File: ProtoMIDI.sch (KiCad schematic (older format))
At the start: 10 parts, among them J1 DIN-5_180degree, U1 6N137

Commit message: Draft schematic (incomplete).
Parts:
- removed C1, C2, C3: 100n, symbol Device:C
- removed D1: 1N4148, symbol Device:D
- removed FB1, FB2: 1k@100MHz, symbol Device:Ferrite_Bead
- removed J1: DIN-5_180degree, symbol Connector:DIN-5_180degree
- removed R1, R2: 220, symbol Device:R
- removed U1: 6N137, Package_DIP:DIP-8_W7.62mm_SMDSocket_SmallPads, symbol Isolator:6N137
- added C10, C11, C14, C15, C21: 1u, Capacitor_SMD:C_0603_1608Metric, symbol Device:C
- added C12, C13: 27p, Capacitor_SMD:C_0603_1608Metric, symbol Device:C
- added C16, C17, C18, C19, C6, C7, C8: 100n, Capacitor_SMD:C_0603_1608Metric, symbol Device:C
- added C20: 10n, Capacitor_SMD:C_0603_1608Metric, symbol Device:C
- added C4: 1u, symbol Device:C
- added C5, C9: 100n, symbol Device:C
- added J10, J12, J13, J14, J15, J16, J17, J18, J19, J3, J4, J5, J6, J7, J8, J9: AudioJack2_SwitchT, Local:PJ398SM, symbol Connector:AudioJack2_SwitchT
- added J11: Conn_01x09_Male, Connector_PinHeader_2.54mm:PinHeader_1x09_P2.54mm_Vertical, symbol Connector:Conn_01x09_Male
- added J2: Conn_01x04_Male, Connector_PinHeader_2.54mm:PinHeader_1x04_P2.54mm_Vertical, symbol Connector:Conn_01x04_Male
- added R10, R11, R12, R13, R14, R15, R16, R8, R9: 1k, Resistor_SMD:R_0603_1608Metric, symbol Device:R
- added R3: 10k, Resistor_SMD:R_0603_1608Metric, symbol Device:R
- added R4: 470, Resistor_SMD:R_0603_1608Metric, symbol Device:R
- added R5, R6, R7: 4k7, Resistor_SMD:R_0603_1608Metric, symbol Device:R
- added SW1: SW_Push, Button_Switch_THT:SW_PUSH_6mm, symbol Switch:SW_Push
- added SW2: SW_Push, symbol Switch:SW_Push
- added SW3: Rotary_Encoder_Switch, Rotary_Encoder:RotaryEncoder_Alps_EC11E-Switch_Vertical_H20mm, symbol Device:Rotary_Encoder_Switch
- added U03: STM32G071RBTx, LQFP64, symbol STM32G071RBTx:STM32G071RBTx
- added U1: AT25xxx, Package_SO:TSSOP-8_4.4x3mm_P0.65mm, symbol Memory_EEPROM:AT25xxx
- added U4: IPS240x240, Local:IPS240x240, symbol Local:IPS240x240
- added U5: 74AHCT244, Package_SO:TSSOP-20_4.4x6.5mm_P0.65mm, symbol 74xx:74HCT244
- added Y1: 8MHz, Crystal:Crystal_SMD_5032-4Pin_5.0x3.2mm, symbol Device:Crystal_GND24_Small
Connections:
- net labels added: +3.3V, +3.3VA, +5V, CV1, CV2, CV3, CV4, CV5, CV6, CV7, CV8, DAC1_CH1, DAC1_CH2, ENC_CH1, ENC_CH2, ENC_SW, GNDA, LED1, LED2, LED3, LED4, LED5, LED6, LED7, LED8, MEM_CS, MEM_MISO, MEM_MOSI, MEM_SCK, RESET, SPI1_MISO, SPI1_MOSI, SPI1_SCK, SPI2_MISO, SPI2_MOSI, SPI2_SCK, SW1, SW2, SW3, SW4, SW5, SW6, SW7, SW8, SWCLK, SWDIO, TFT+, TFT-, TFT_DC, TFT_RES, TRIG0, TRIG1, TRIG2, TRIG3, TRIG4, TRIG5, TRIG6, TRIG7, TRIG8, USART3_RX, USART3_TX, VREF
- wire segments 32 -> 238
- no-connect marks 0 -> 16
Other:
- note removed: "FIXME: Connect\ncase here!"

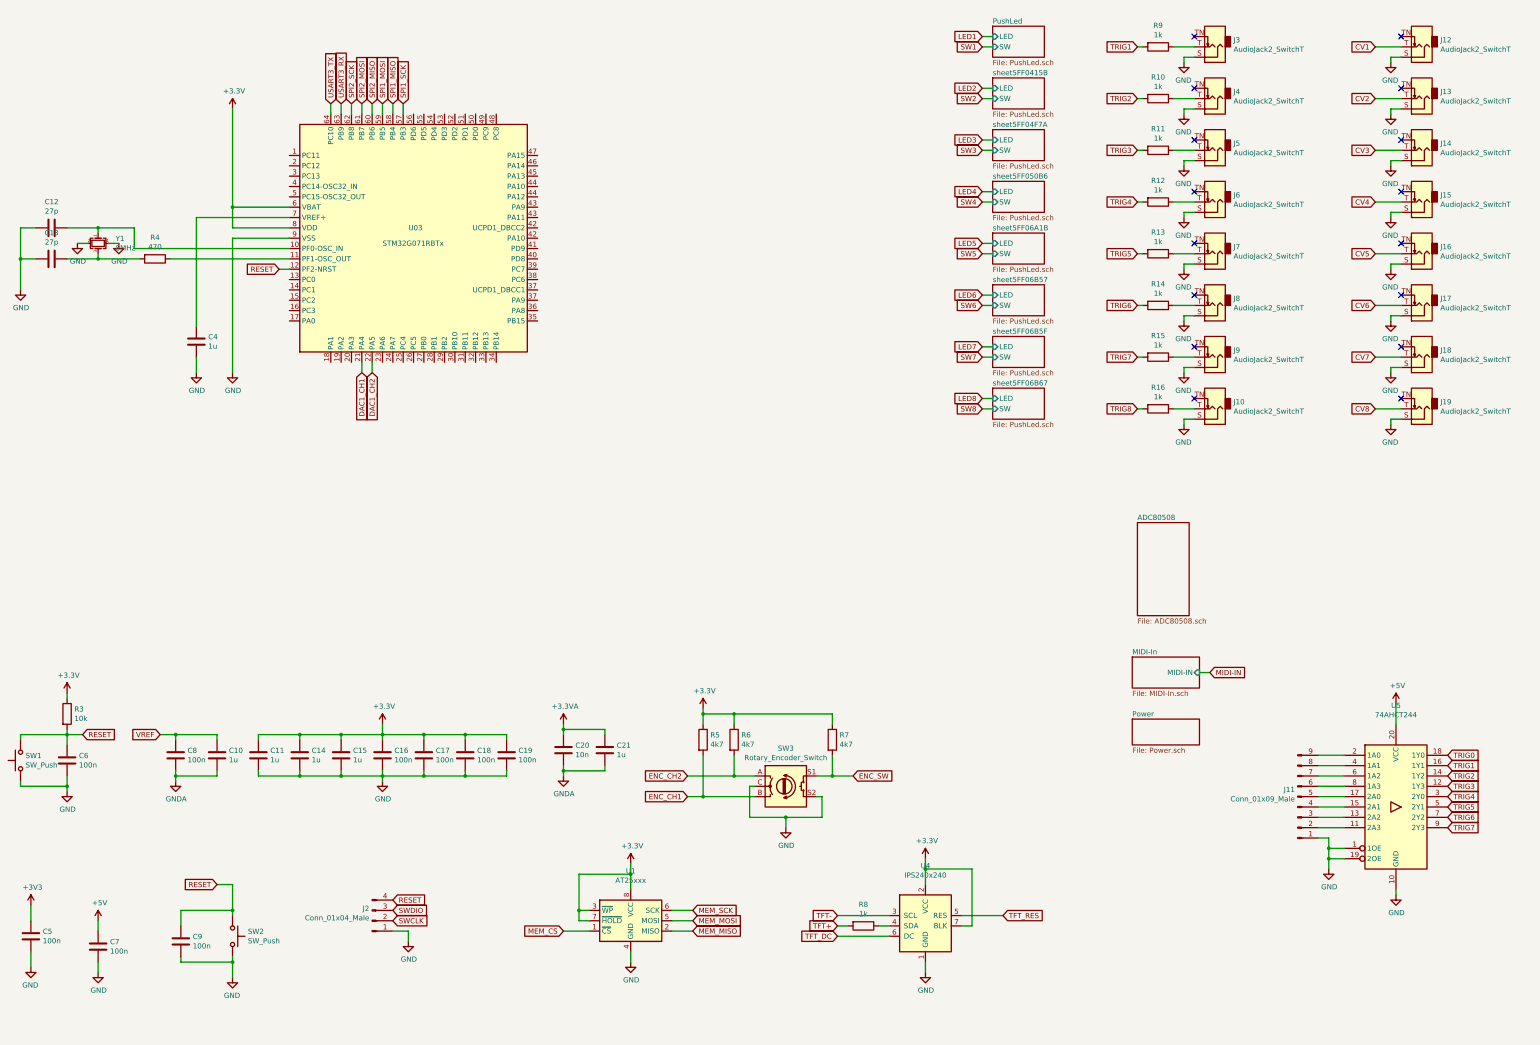
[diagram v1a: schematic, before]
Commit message: Use 48-pin package.
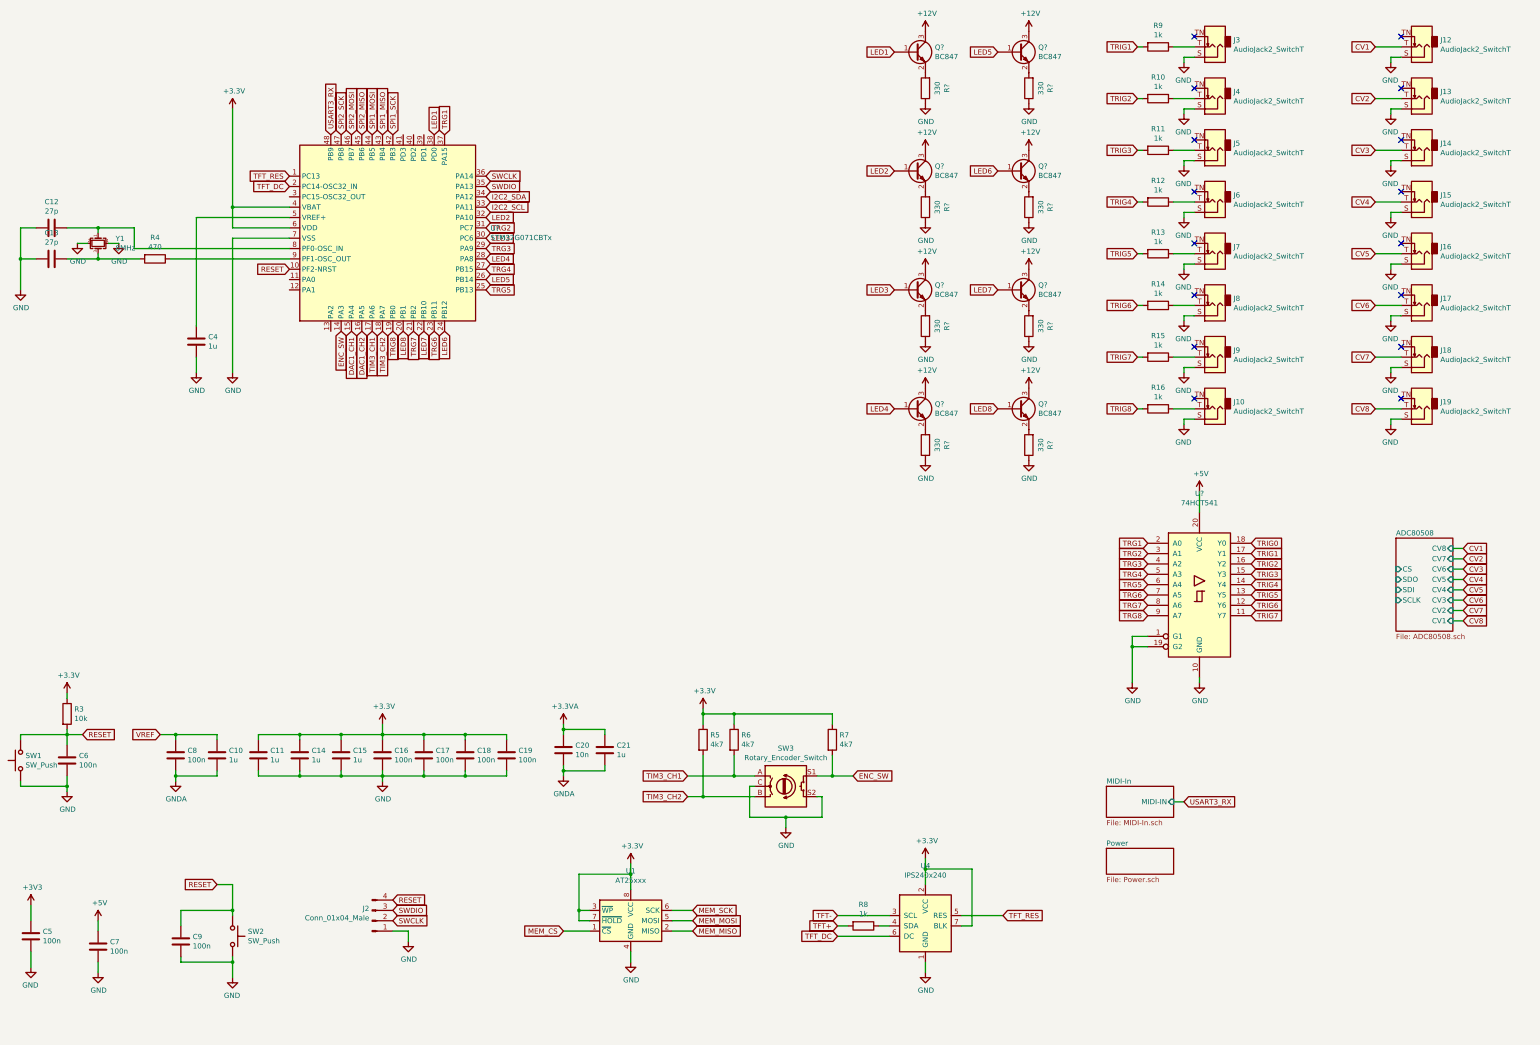
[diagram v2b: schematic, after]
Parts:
- removed J11: Conn_01x09_Male, Connector_PinHeader_2.54mm:PinHeader_1x09_P2.54mm_Vertical, symbol Connector:Conn_01x09_Male
- removed U03: STM32G071RBTx, LQFP64, symbol STM32G071RBTx:STM32G071RBTx
- removed U5: 74AHCT244, Package_SO:TSSOP-20_4.4x6.5mm_P0.65mm, symbol 74xx:74HCT244
- added Q? (x8): BC847, Package_TO_SOT_SMD:SOT-23, symbol Transistor_BJT:BC847
- added R? (x8): 330, Resistor_SMD:R_0603_1608Metric, symbol Device:R
- added U?: 74HCT541, symbol 74xx:74HCT541
- added U?: STM32G071CBTx, LQFP48, symbol STM32G071CBTx:STM32G071CBTx
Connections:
- net +3V3: now also U?.4 (VBAT), U?.6 (VDD)
- net +5V: now also U?.20 (VCC)
- net DAC1_CH1: now also U?.15 (PA4)
- net DAC1_CH2: now also U?.16 (PA5)
- net ENC_SW: now also U?.14 (PA3)
- net GND: now also R?.1, R?.1, R?.1, R?.1, R?.1, R?.1, R?.1, R?.1, U?.1 (G1), U?.10 (GND), U?.19 (G2), U?.7 (VSS)
- net LED1: now also Q?.1 (B), U?.38 (PD0)
- net LED2: now also Q?.1 (B), U?.32 (PA10)
- net LED3: now also Q?.1 (B), U?.30 (PC6)
- net LED4: now also Q?.1 (B), U?.28 (PA8)
- net LED5: now also Q?.1 (B), U?.26 (PB14)
- net LED6: now also Q?.1 (B), U?.24 (PB12)
- net LED7: now also Q?.1 (B), U?.22 (PB10)
- net LED8: now also Q?.1 (B), U?.20 (PB1)
- net RESET: now also U?.10 (PF2-NRST)
- net SPI1_MISO: now also U?.43 (PB4)
- net SPI1_MOSI: now also U?.44 (PB5)
- net SPI1_SCK: now also U?.42 (PB3)
- net SPI2_MISO: now also U?.45 (PB6)
- net SPI2_MOSI: now also U?.46 (PB7)
- net SPI2_SCK: now also U?.47 (PB8)
- net SWCLK: now also U?.36 (PA14)
- net SWDIO: now also U?.35 (PA13)
- net TFT_DC: now also U?.2 (PC14-OSC32_IN)
- net TFT_RES: now also U?.1 (PC13)
- net TRIG0: now also U?.18 (Y0)
- net TRIG1: now also U?.17 (Y1)
- net TRIG2: now also U?.16 (Y2)
- net TRIG3: now also U?.15 (Y3)
- net TRIG4: now also U?.14 (Y4)
- net TRIG5: now also U?.13 (Y5)
- net TRIG6: now also U?.12 (Y6)
- net TRIG7: now also U?.11 (Y7)
- net USART3_RX: now also U?.48 (PB9)
- net at C4.1: now also U?.5 (VREF+)
- net at C12.1, Y1.1: now also U?.8 (PF0-OSC_IN)
- net at R4.1: now also U?.9 (PF1-OSC_OUT)
- net ENC_CH1 renamed TIM3_CH2
- net TIM3_CH2: now also U?.18 (PA7)
- net ENC_CH2 renamed TIM3_CH1
- net TIM3_CH1: now also U?.17 (PA6)
- new net: Q?.2 (E), R?.2 (x8)
- new net +12V: Q?.3 (C), Q?.3 (C), Q?.3 (C), Q?.3 (C), Q?.3 (C), Q?.3 (C), Q?.3 (C), Q?.3 (C)
- new net I2C2_SCL: U?.33 (PA11)
- new net I2C2_SDA: U?.34 (PA12)
- new net TRG1: U?.2 (A0), U?.37 (PA15)
- new net TRG2: U?.3 (A1), U?.31 (PC7)
- new net TRG3: U?.29 (PA9), U?.4 (A2)
- new net TRG4: U?.27 (PB15), U?.5 (A3)
- new net TRG5: U?.25 (PB13), U?.6 (A4)
- new net TRG6: U?.23 (PB11), U?.7 (A5)
- new net TRG7: U?.21 (PB2), U?.8 (A6)
- new net TRG8: U?.19 (PB0), U?.9 (A7)

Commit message: Designed velocity CV section.
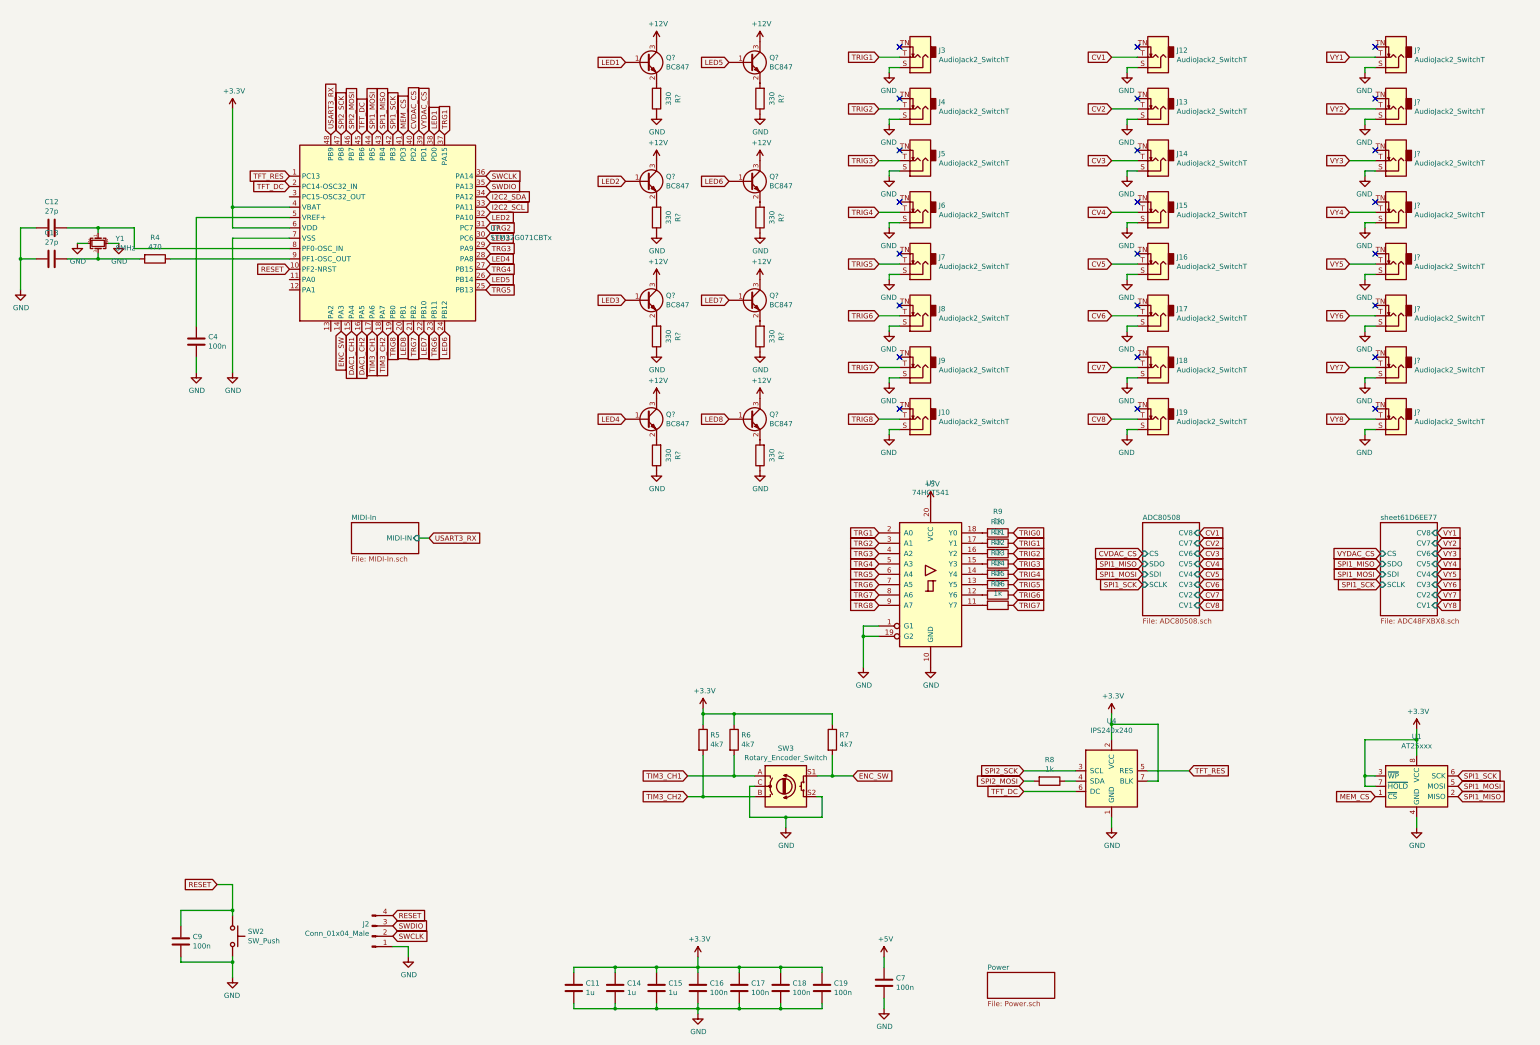
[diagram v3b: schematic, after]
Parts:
- removed C10, C21: 1u, Capacitor_SMD:C_0603_1608Metric, symbol Device:C
- removed C20: 10n, Capacitor_SMD:C_0603_1608Metric, symbol Device:C
- removed C5: 100n, symbol Device:C
- removed C6, C8: 100n, Capacitor_SMD:C_0603_1608Metric, symbol Device:C
- removed R3: 10k, Resistor_SMD:R_0603_1608Metric, symbol Device:R
- removed SW1: SW_Push, Button_Switch_THT:SW_PUSH_6mm, symbol Switch:SW_Push
- added J? (x8): AudioJack2_SwitchT, Local:PJ398SM, symbol Connector:AudioJack2_SwitchT
- C4: value 1u -> 100n
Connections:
- net MEM_MISO is gone; now on net SPI1_MISO: U1.2 (MISO)
- net MEM_MOSI is gone; now on net SPI1_MOSI: U1.5 (MOSI)
- net MEM_SCK is gone; now on net SPI1_SCK: U1.6 (SCK)
- net SPI2_MISO is gone; now on net TFT_DC: U?.45 (PB6)
- net TFT+ is gone; now on net SPI2_MOSI: R8.2
- net TFT- is gone; now on net SPI2_SCK: U4.3 (SCL)
- net GND: now also J?.S, J?.S, J?.S, J?.S, J?.S, J?.S, J?.S, J?.S
- net MEM_CS: now also U?.41 (PD3)
- net TRIG0: now also R9.1; no longer U?.18 (Y0)
- net TRIG1: now also J3.T, R10.1; no longer R9.2, U?.17 (Y1)
- net TRIG2: now also J4.T, R11.1; no longer R10.2, U?.16 (Y2)
- net TRIG3: now also J5.T, R12.1; no longer R11.2, U?.15 (Y3)
- net TRIG4: now also J6.T, R13.1; no longer R12.2, U?.14 (Y4)
- net TRIG5: now also J7.T, R14.1; no longer R13.2, U?.13 (Y5)
- net TRIG6: now also J8.T, R15.1; no longer R14.2, U?.12 (Y6)
- net TRIG7: now also J9.T, R16.1; no longer R15.2, U?.11 (Y7)
- net TRIG8: now also J10.T; no longer R16.2
- net VYDAC_CS: now reaches U?.39 (PD1)
- net CVDAC_CS: now reaches U?.40 (PD2)
- new net: R9.2, U?.18 (Y0)
- new net: R10.2, U?.17 (Y1)
- new net: R11.2, U?.16 (Y2)
- new net: R12.2, U?.15 (Y3)
- new net: R13.2, U?.14 (Y4)
- new net: R14.2, U?.13 (Y5)
- new net: R15.2, U?.12 (Y6)
- new net: R16.2, U?.11 (Y7)
- new net VY1: J?.T
- new net VY2: J?.T
- new net VY3: J?.T
- new net VY4: J?.T
- new net VY5: J?.T
- new net VY6: J?.T
- new net VY7: J?.T
- new net VY8: J?.T
- no-connect marks 16 -> 24
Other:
- moved on the sheet: C11, C14, C15, C16, C17, C18, C19, C7, J10, J12, J13, J14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
